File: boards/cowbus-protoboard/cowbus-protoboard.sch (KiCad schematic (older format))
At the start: 2 parts

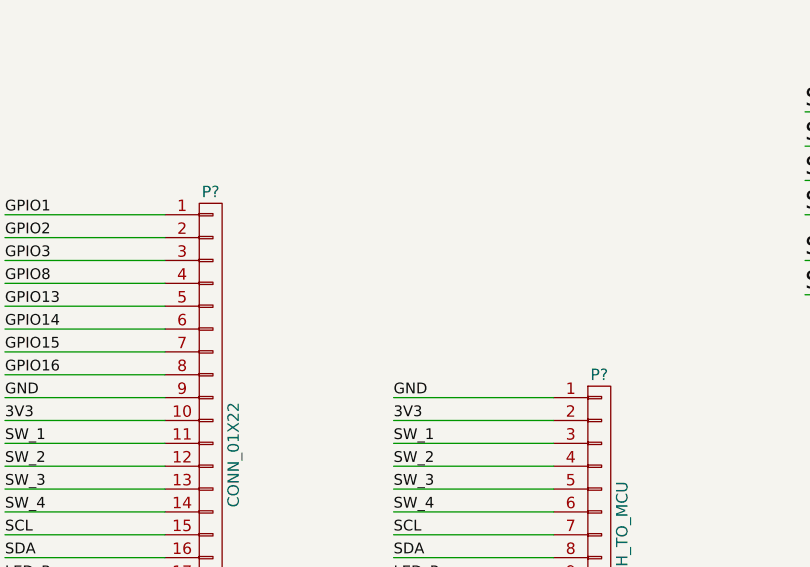
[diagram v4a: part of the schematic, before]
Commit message: some footprint assignments done
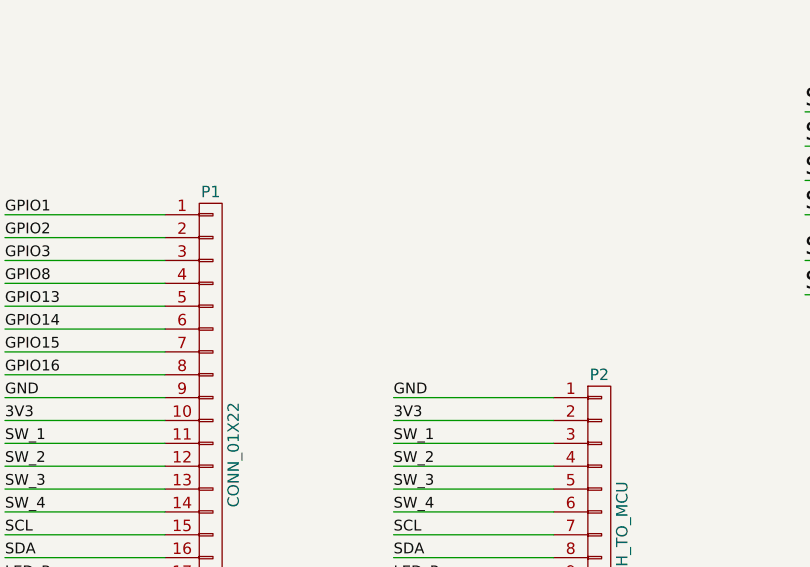
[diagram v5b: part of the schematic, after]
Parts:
- P1: renamed from P?; footprint (none) -> Pin_Headers:Pin_Header_Straight_1x22
- P2: renamed from P?; footprint (none) -> Pin_Headers:Pin_Header_Straight_1x14
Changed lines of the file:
@@
 LED_B
 $Comp
-L VCC #PWR?
+L VCC #PWR01
 U 1 1 55A6ED40
 P 1150 1300
-F 0 "#PWR?" H 1150 1150 50  0001 C CNN
+F 0 "#PWR01" H 1150 1150 50  0001 C CNN
 F 1 "VCC" H 1150 1450 50  0000 C CNN
 F 2 "" H 1150 1300 60  0000 C CNN
@@
 $EndComp
 $Comp
-L VCC #PWR?
+L VCC #PWR02
 U 1 1 55A73D74
 P 4900 1300
-F 0 "#PWR?" H 4900 1150 50  0001 C CNN
+F 0 "#PWR02" H 4900 1150 50  0001 C CNN
 F 1 "VCC" H 4900 1450 50  0000 C CNN
 F 2 "" H 4900 1300 60  0000 C CNN
@@
 $EndComp
 $Comp
-L +3V3 #PWR?
+L +3V3 #PWR03
 U 1 1 55A75A13
 P 8550 1700
-F 0 "#PWR?" H 8550 1550 50  0001 C CNN
+F 0 "#PWR03" H 8550 1550 50  0001 C CNN
 F 1 "+3V3" H 8550 1840 50  0000 C CNN
 F 2 "" H 8550 1700 60  0000 C CNN
@@
 SDA
 $Comp
-L CONN_01X14 P?
+L CONN_01X14 P2
 U 1 1 55A86865
 P 3800 6500
-F 0 "P?" H 3800 7250 50  0000 C CNN
+F 0 "P2" H 3800 7250 50  0000 C CNN
 F 1 "PERIPH_TO_MCU" V 3900 6500 50  0000 C CNN
-F 2 "" H 3800 6500 60  0000 C CNN
+F 2 "Pin_Headers:Pin_Header_Straight_1x14" H 3800 6500 60  0001 C CNN
 F 3 "" H 3800 6500 60  0000 C CNN
 	1    3800 6500
@@
 GPIO14
 $Comp
-L CONN_01X22 P?
+L CONN_01X22 P1
 U 1 1 55A93700
 P 2100 6100
-F 0 "P?" H 2100 7250 50  0000 C CNN
+F 0 "P1" H 2100 7250 50  0000 C CNN
 F 1 "CONN_01X22" V 2200 6100 50  0000 C CNN
-F 2 "" H 2100 6100 60  0000 C CNN
+F 2 "Pin_Headers:Pin_Header_Straight_1x22" H 2100 6100 60  0001 C CNN
 F 3 "" H 2100 6100 60  0000 C CNN
 	1    2100 6100

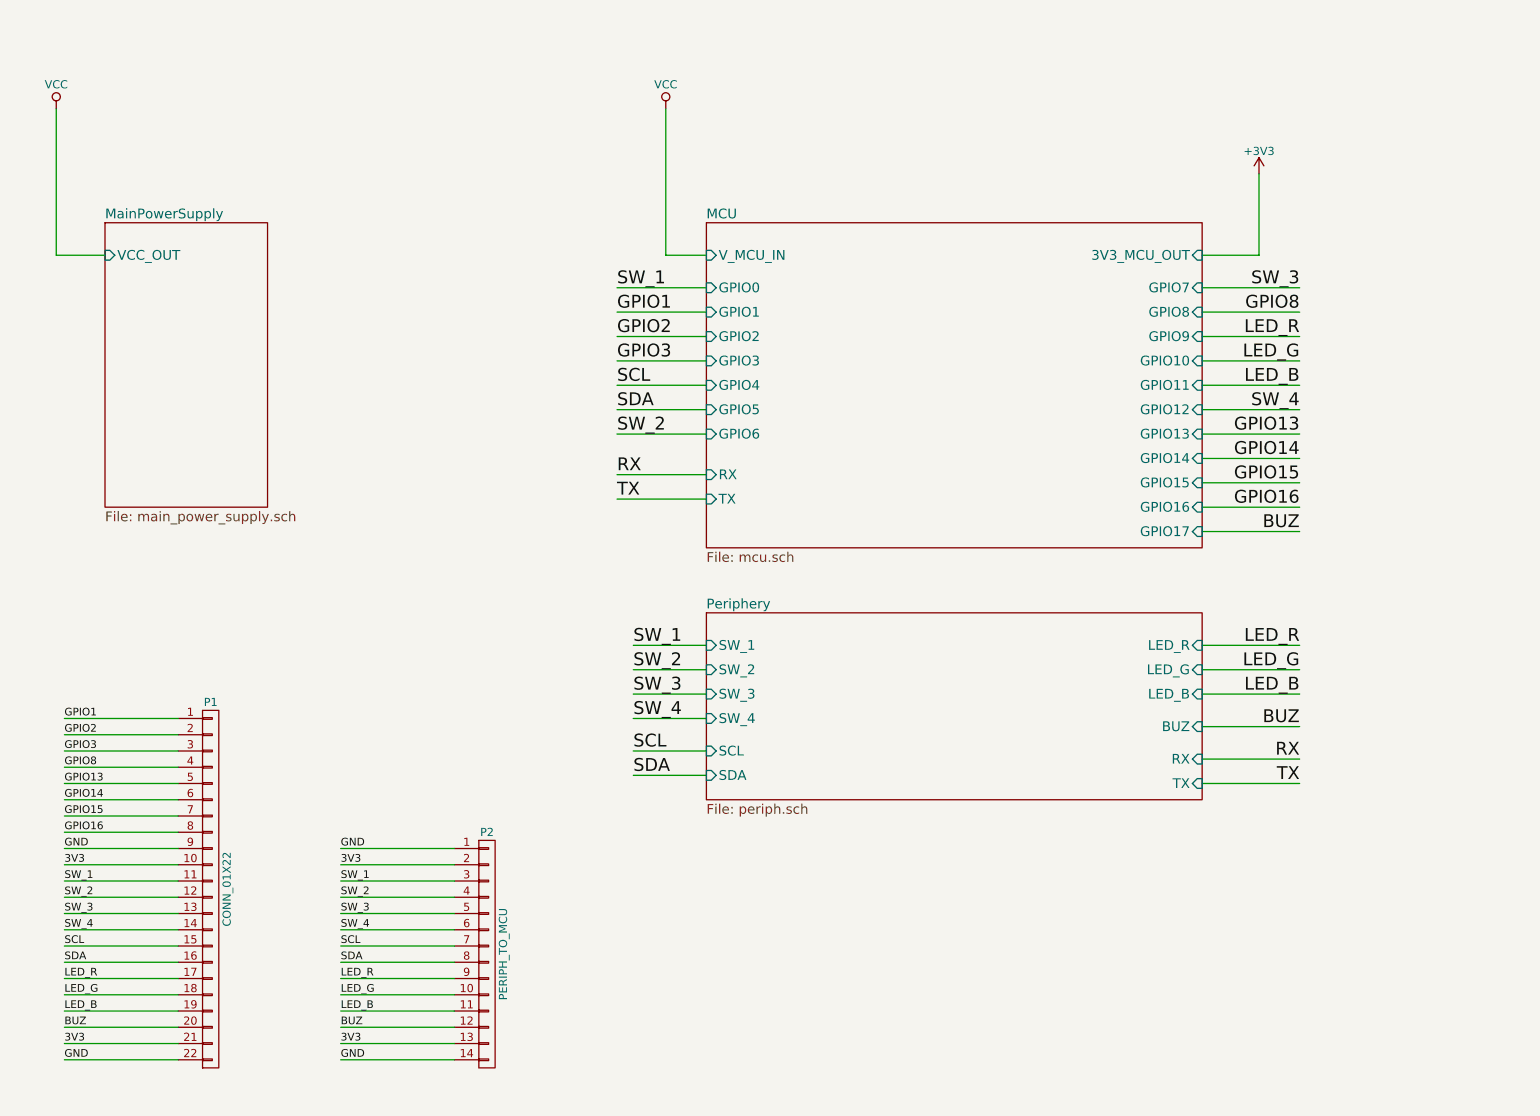
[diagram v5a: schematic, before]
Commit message: first version of layout for protoboard
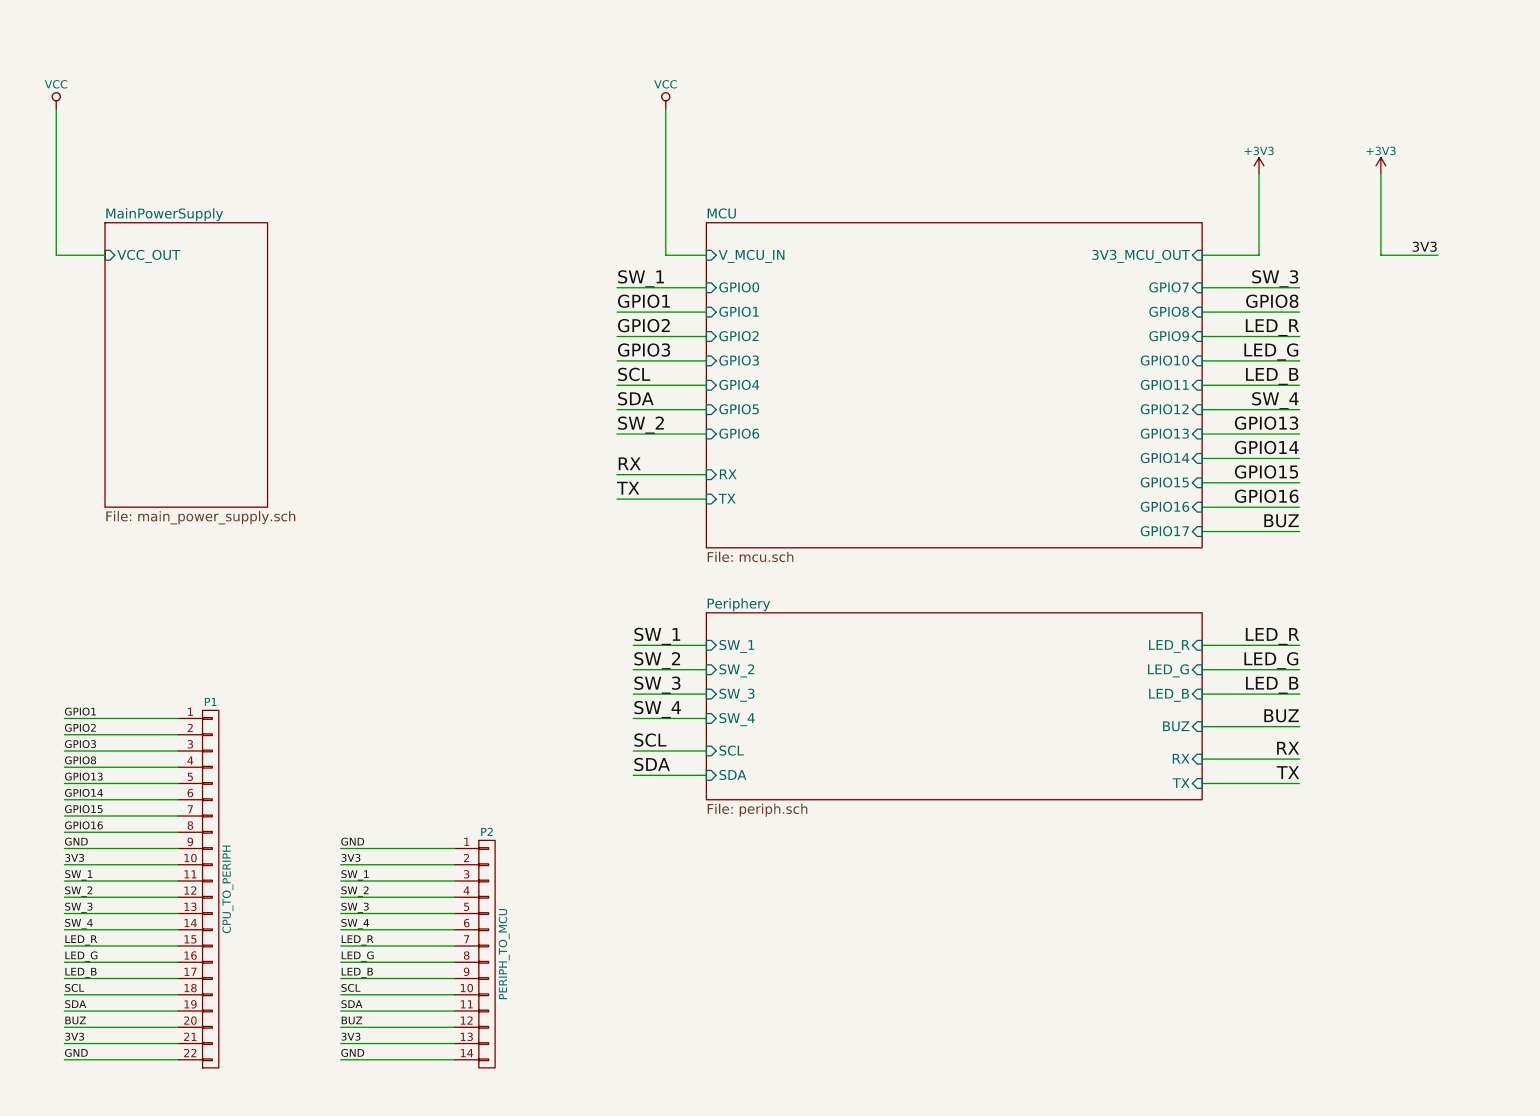
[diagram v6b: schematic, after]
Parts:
- P1: value CONN_01X22 -> CPU_TO_PERIPH
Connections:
- net 3V3 is gone; now on net +3V3: P1.10 (P10), P1.21 (P21), P2.13 (P13), P2.2 (P2)
- net LED_B: now also P1.17 (P17), P2.9 (P9); no longer P1.19 (P19), P2.11 (P11)
- net LED_G: now also P1.16 (P16), P2.8 (P8); no longer P1.18 (P18), P2.10 (P10)
- net LED_R: now also P1.15 (P15), P2.7 (P7); no longer P1.17 (P17), P2.9 (P9)
- net SCL: now also P1.18 (P18), P2.10 (P10); no longer P1.15 (P15), P2.7 (P7)
- net SDA: now also P1.19 (P19), P2.11 (P11); no longer P1.16 (P16), P2.8 (P8)
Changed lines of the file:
@@
 EESchema Schematic File Version 2
+LIBS:cowbus-protoboard-rescue
 LIBS:power
 LIBS:device
@@
 LIBS:nrf24l01plus-module
 LIBS:i2c
+LIBS:led_rgb_reichelt
 LIBS:cowbus-protoboard-cache
 EELAYER 25 0
@@
 LED_B
 $Comp
-L VCC #PWR01
+L VCC #PWR1
 U 1 1 55A6ED40
 P 1150 1300
-F 0 "#PWR01" H 1150 1150 50  0001 C CNN
+F 0 "#PWR1" H 1150 1150 50  0001 C CNN
 F 1 "VCC" H 1150 1450 50  0000 C CNN
 F 2 "" H 1150 1300 60  0000 C CNN
@@
 $EndComp
 $Comp
-L VCC #PWR02
+L VCC #PWR2
 U 1 1 55A73D74
 P 4900 1300
-F 0 "#PWR02" H 4900 1150 50  0001 C CNN
+F 0 "#PWR2" H 4900 1150 50  0001 C CNN
 F 1 "VCC" H 4900 1450 50  0000 C CNN
 F 2 "" H 4900 1300 60  0000 C CNN
@@
 $EndComp
 $Comp
-L +3V3 #PWR03
+L +3V3 #PWR3
 U 1 1 55A75A13
 P 8550 1700
-F 0 "#PWR03" H 8550 1550 50  0001 C CNN
+F 0 "#PWR3" H 8550 1550 50  0001 C CNN
 F 1 "+3V3" H 8550 1840 50  0000 C CNN
 F 2 "" H 8550 1700 60  0000 C CNN
@@
 	3600 6350 2900 6350
 Wire Wire Line
+	3600 6750 2900 6750
+Wire Wire Line
+	3600 6850 2900 6850
+Wire Wire Line
 	3600 6450 2900 6450
 Wire Wire Line
@@
 Wire Wire Line
 	3600 6650 2900 6650
-Wire Wire Line
-	3600 6750 2900 6750
-Wire Wire Line
-	3600 6850 2900 6850
 Wire Wire Line
 	3600 6950 2900 6950
@@
 Text Label 2900 6350 0    47   ~ 0
 SW_4
+Text Label 2900 6750 0    47   ~ 0
+SCL
+Text Label 2900 6850 0    47   ~ 0
+SDA
 Text Label 2900 6450 0    47   ~ 0
-SCL
+LED_R
 Text Label 2900 6550 0    47   ~ 0
-SDA
+LED_G
 Text Label 2900 6650 0    47   ~ 0
-LED_R
-Text Label 2900 6750 0    47   ~ 0
-LED_G
-Text Label 2900 6850 0    47   ~ 0
 LED_B
 Text Label 2900 6950 0    47   ~ 0
@@
 	1900 6350 1200 6350
 Wire Wire Line
+	1900 6750 1200 6750
+Wire Wire Line
+	1900 6850 1200 6850
+Wire Wire Line
 	1900 6450 1200 6450
 Wire Wire Line
@@
 Wire Wire Line
 	1900 6650 1200 6650
-Wire Wire Line
-	1900 6750 1200 6750
-Wire Wire Line
-	1900 6850 1200 6850
 Wire Wire Line
 	1900 6950 1200 6950
@@
 Text Label 1200 6350 0    47   ~ 0
 SW_4
+Text Label 1200 6750 0    47   ~ 0
+SCL
+Text Label 1200 6850 0    47   ~ 0
+SDA
 Text Label 1200 6450 0    47   ~ 0
-SCL
+LED_R
 Text Label 1200 6550 0    47   ~ 0
-SDA
+LED_G
 Text Label 1200 6650 0    47   ~ 0
-LED_R
-Text Label 1200 6750 0    47   ~ 0
-LED_G
-Text Label 1200 6850 0    47   ~ 0
 LED_B
 Text Label 1200 6950 0    47   ~ 0
@@
 P 2100 6100
 F 0 "P1" H 2100 7250 50  0000 C CNN
-F 1 "CONN_01X22" V 2200 6100 50  0000 C CNN
+F 1 "CPU_TO_PERIPH" V 2200 6100 50  0000 C CNN
 F 2 "Pin_Headers:Pin_Header_Straight_1x22" H 2100 6100 60  0001 C CNN
 F 3 "" H 2100 6100 60  0000 C CNN
@@
 Text Label 8800 5450 2    79   ~ 0
 TX
+$Comp
+L +3V3 #PWR4
+U 1 1 55BE898C
+P 9300 1700
+F 0 "#PWR4" H 9300 1550 50  0001 C CNN
+F 1 "+3V3" H 9300 1840 50  0000 C CNN
+F 2 "" H 9300 1700 60  0000 C CNN
+F 3 "" H 9300 1700 60  0000 C CNN
+	1    9300 1700
+	-1   0    0    -1
+$EndComp
+Wire Wire Line
+	9650 2200 9300 2200
+Wire Wire Line
+	9300 2200 9300 1700
+Text Label 9650 2200 2    60   ~ 0
+3V3
 $EndSCHEMATC
